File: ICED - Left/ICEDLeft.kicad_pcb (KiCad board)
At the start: 2 copper layers, 175.4 x 145 mm, 164 parts, among them P1 FLASH_HDR, P2 USBC, P3 CONN_17, P4 USB3_AFEMALE, Q1 TC1264, U1 MK20DX256VLH7, U2 IS31FL3731C, X1 CRYSTAL

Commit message: moved S23
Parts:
- moved D23 2.41 mm to (144.9, 94.6)
- moved D61 2.41 mm to (150.0, 97.7)
- moved S23 2.41 mm to (144.9, 97.7)
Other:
- outline, holes or cut-outs redrawn
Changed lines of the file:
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@@
   )
   (module prettylib:INSW_LEDS_REG (layer Front)
-    (at 149.987 100.086 270)
+    (at 149.9952 97.672 270)
     (attr smd)
     (fp_text reference D61 (at 0 -1.5 270) (layer B.SilkS)
@@
   )
   (module prettylib:SOT123-DIODE (layer Back)
-    (at 144.907 96.9745 90)
+    (at 144.9152 94.5605 90)
     (descr DIODE)
     (tags DIODE)
@@
   )
   (module prettylib:MXALPS (layer Front)
-    (at 144.907 100.086 90)
+    (at 144.9152 97.672 90)
     (descr MXALPS)
     (tags MXALPS)
@@
   (gr_line (start 170.053 170.815) (end 170.434 170.815) (angle 90) (layer Edge.Cuts) (width 0.127))
   (gr_line (start 193.04 122.301) (end 170.434 170.815) (angle 90) (layer Edge.Cuts) (width 0.127))
-  (gr_line (start 90.17 135.509) (end 94.361 135.509) (angle 90) (layer Edge.Cuts) (width 0.127))
-  (gr_line (start 170.053 170.815) (end 94.361 135.509) (angle 90) (layer Edge.Cuts) (width 0.127))
+  (gr_line (start 66.012873 135.509) (end 66.012873 164.658583) (angle 90) (layer Edge.Cuts) (width 0.127))
+  (gr_line (start 66.012873 164.658583) (end 94.361 170.815) (angle 90) (layer Edge.Cuts) (width 0.127))
   (gr_line (start 192.913 122.047) (end 154.813 104.267) (angle 90) (layer Edge.Cuts) (width 0.127))
-  (gr_line (start 90.17 135.509) (end 20.955 135.509) (angle 90) (layer Edge.Cuts) (width 0.127))
+  (gr_line (start 66.012873 135.509) (end 20.955 135.509) (angle 90) (layer Edge.Cuts) (width 0.127))
   (gr_line (start 64.897 27.559) (end 19.558 27.559) (angle 90) (layer Edge.Cuts) (width 0.127))
   (gr_line (start 64.897 32.639) (end 64.897 27.559) (angle 90) (layer Edge.Cuts) (width 0.127))

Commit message: moved LCD1
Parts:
- moved LCD1 135.8 mm to (157.6, 104.0), turned to 270 degrees
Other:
- outline, holes or cut-outs redrawn
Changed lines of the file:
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@@
   )
   (module prettylib:NHD-C12832A1Z (layer Front)
-    (at 38.497 38.615)
+    (at 157.58588 103.96079 270)
     (descr "NHD-C12832A1Z LCD")
     (tags "HDR SIL")
-    (fp_text reference LCD1 (at 23.098 -5.976) (layer F.SilkS)
+    (fp_text reference LCD1 (at 23.098 -5.976 90) (layer F.SilkS)
       (effects (font (size 1 1) (thickness 0.2)))
     )
-    (fp_text value NHD-C12832A1Z (at 0 2.1) (layer F.SilkS) hide
+    (fp_text value NHD-C12832A1Z (at 0 2.1 90) (layer F.SilkS) hide
       (effects (font (size 0.65 0.65) (thickness 0.0975)))
     )
@@
     (fp_line (start -20.7 -23.7) (end -20.7 0.6) (layer Dwgs.User) (width 0.3))
     (fp_line (start 20.7 0.6) (end 20.7 -23.7) (layer Dwgs.User) (width 0.3))
-    (pad 1 thru_hole rect (at -17.3 -1.95 90) (size 1.5 2.4) (drill oval 0.9 2) (layers *.Cu *.Mask F.SilkS)
+    (pad 1 thru_hole rect (at -17.3 -1.95 0) (size 1.5 2.4) (drill oval 0.9 2) (layers *.Cu *.Mask F.SilkS)
       (net 33 VDD))
-    (pad 2 thru_hole rect (at -14.3 -1.95 90) (size 1.5 2.4) (drill oval 0.9 2) (layers *.Cu *.Mask F.SilkS)
+    (pad 2 thru_hole rect (at -14.3 -1.95 0) (size 1.5 2.4) (drill oval 0.9 2) (layers *.Cu *.Mask F.SilkS)
       (net 89 "Net-(LCD1-Pad2)"))
-    (pad 3 thru_hole circle (at -12 0 90) (size 1.2 1.2) (drill 0.7) (layers *.Cu *.Mask F.SilkS)
+    (pad 3 thru_hole circle (at -12 0 0) (size 1.2 1.2) (drill 0.7) (layers *.Cu *.Mask F.SilkS)
       (net 48 "Net-(C17-Pad2)"))
-    (pad 4 thru_hole circle (at -10.5 0 90) (size 1.2 1.2) (drill 0.7) (layers *.Cu *.Mask F.SilkS)
+    (pad 4 thru_hole circle (at -10.5 0 0) (size 1.2 1.2) (drill 0.7) (layers *.Cu *.Mask F.SilkS)
       (net 47 "Net-(C16-Pad2)"))
-    (pad 5 thru_hole circle (at -9 0 90) (size 1.2 1.2) (drill 0.7) (layers *.Cu *.Mask F.SilkS)
+    (pad 5 thru_hole circle (at -9 0 0) (size 1.2 1.2) (drill 0.7) (layers *.Cu *.Mask F.SilkS)
       (net 46 "Net-(C15-Pad2)"))
-    (pad 6 thru_hole circle (at -7.5 0 90) (size 1.2 1.2) (drill 0.7) (layers *.Cu *.Mask F.SilkS)
+    (pad 6 thru_hole circle (at -7.5 0 0) (size 1.2 1.2) (drill 0.7) (layers *.Cu *.Mask F.SilkS)
       (net 45 "Net-(C14-Pad2)"))
-    (pad 7 thru_hole circle (at -6 0 90) (size 1.2 1.2) (drill 0.7) (layers *.Cu *.Mask F.SilkS)
+    (pad 7 thru_hole circle (at -6 0 0) (size 1.2 1.2) (drill 0.7) (layers *.Cu *.Mask F.SilkS)
       (net 44 "Net-(C13-Pad2)"))
-    (pad 8 thru_hole circle (at -4.5 0 90) (size 1.2 1.2) (drill 0.7) (layers *.Cu *.Mask F.SilkS)
+    (pad 8 thru_hole circle (at -4.5 0 0) (size 1.2 1.2) (drill 0.7) (layers *.Cu *.Mask F.SilkS)
       (net 43 "Net-(C12-Pad2)"))
-    (pad 9 thru_hole circle (at -3 0 90) (size 1.2 1.2) (drill 0.7) (layers *.Cu *.Mask F.SilkS)
+    (pad 9 thru_hole circle (at -3 0 0) (size 1.2 1.2) (drill 0.7) (layers *.Cu *.Mask F.SilkS)
       (net 42 "Net-(C12-Pad1)"))
-    (pad 10 thru_hole circle (at -1.5 0 90) (size 1.2 1.2) (drill 0.7) (layers *.Cu *.Mask F.SilkS)
+    (pad 10 thru_hole circle (at -1.5 0 0) (size 1.2 1.2) (drill 0.7) (layers *.Cu *.Mask F.SilkS)
       (net 41 "Net-(C11-Pad2)"))
-    (pad 11 thru_hole circle (at 0 0 90) (size 1.2 1.2) (drill 0.7) (layers *.Cu *.Mask F.SilkS)
+    (pad 11 thru_hole circle (at 0 0 0) (size 1.2 1.2) (drill 0.7) (layers *.Cu *.Mask F.SilkS)
       (net 40 "Net-(C11-Pad1)"))
-    (pad 12 thru_hole circle (at 1.5 0 90) (size 1.2 1.2) (drill 0.7) (layers *.Cu *.Mask F.SilkS)
+    (pad 12 thru_hole circle (at 1.5 0 0) (size 1.2 1.2) (drill 0.7) (layers *.Cu *.Mask F.SilkS)
       (net 39 "Net-(C10-Pad1)"))
-    (pad 13 thru_hole circle (at 3 0 90) (size 1.2 1.2) (drill 0.7) (layers *.Cu *.Mask F.SilkS)
+    (pad 13 thru_hole circle (at 3 0 0) (size 1.2 1.2) (drill 0.7) (layers *.Cu *.Mask F.SilkS)
       (net 34 VSS))
-    (pad 14 thru_hole circle (at 4.5 0 90) (size 1.2 1.2) (drill 0.7) (layers *.Cu *.Mask F.SilkS)
+    (pad 14 thru_hole circle (at 4.5 0 0) (size 1.2 1.2) (drill 0.7) (layers *.Cu *.Mask F.SilkS)
       (net 33 VDD))
-    (pad 15 thru_hole circle (at 6 0 90) (size 1.2 1.2) (drill 0.7) (layers *.Cu *.Mask F.SilkS)
+    (pad 15 thru_hole circle (at 6 0 0) (size 1.2 1.2) (drill 0.7) (layers *.Cu *.Mask F.SilkS)
       (net 16 /mcu/MOSI))
-    (pad 16 thru_hole circle (at 7.5 0 90) (size 1.2 1.2) (drill 0.7) (layers *.Cu *.Mask F.SilkS)
+    (pad 16 thru_hole circle (at 7.5 0 0) (size 1.2 1.2) (drill 0.7) (layers *.Cu *.Mask F.SilkS)
       (net 22 /mcu/SCLK))
-    (pad 17 thru_hole circle (at 9 0 90) (size 1.2 1.2) (drill 0.7) (layers *.Cu *.Mask F.SilkS)
+    (pad 17 thru_hole circle (at 9 0 0) (size 1.2 1.2) (drill 0.7) (layers *.Cu *.Mask F.SilkS)
       (net 11 /mcu/A0))
-    (pad 18 thru_hole circle (at 10.5 0 90) (size 1.2 1.2) (drill 0.7) (layers *.Cu *.Mask F.SilkS)
+    (pad 18 thru_hole circle (at 10.5 0 0) (size 1.2 1.2) (drill 0.7) (layers *.Cu *.Mask F.SilkS)
       (net 17 /mcu/RST))
-    (pad 19 thru_hole circle (at 12 0 90) (size 1.2 1.2) (drill 0.7) (layers *.Cu *.Mask F.SilkS)
+    (pad 19 thru_hole circle (at 12 0 0) (size 1.2 1.2) (drill 0.7) (layers *.Cu *.Mask F.SilkS)
       (net 25 /mcu/SS1))
-    (pad 20 thru_hole rect (at 14.3 -1.95 90) (size 1.5 2.4) (drill oval 0.9 2) (layers *.Cu *.Mask F.SilkS)
+    (pad 20 thru_hole rect (at 14.3 -1.95 0) (size 1.5 2.4) (drill oval 0.9 2) (layers *.Cu *.Mask F.SilkS)
       (net 90 "Net-(LCD1-Pad20)"))
-    (pad 21 thru_hole rect (at 17.3 -1.95 90) (size 1.5 2.4) (drill oval 0.9 2) (layers *.Cu *.Mask F.SilkS)
+    (pad 21 thru_hole rect (at 17.3 -1.95 0) (size 1.5 2.4) (drill oval 0.9 2) (layers *.Cu *.Mask F.SilkS)
       (net 91 "Net-(LCD1-Pad21)"))
-    (pad "" np_thru_hole circle (at 20.1 0 90) (size 0.85001 0.85001) (drill 0.85) (layers *.Cu *.Mask F.SilkS))
-    (pad "" np_thru_hole circle (at -20.1 0 90) (size 0.85001 0.85001) (drill 0.85) (layers *.Cu *.Mask F.SilkS))
+    (pad "" np_thru_hole circle (at 20.1 0 0) (size 0.85001 0.85001) (drill 0.85) (layers *.Cu *.Mask F.SilkS))
+    (pad "" np_thru_hole circle (at -20.1 0 0) (size 0.85001 0.85001) (drill 0.85) (layers *.Cu *.Mask F.SilkS))
     (model 3d/NHD-C12832A1Z.wrl
-      (at (xyz 0 -0.024 0.065))
+      (at (xyz 0 -0.024 270.065))
       (scale (xyz 0.393701 0.393701 0.393701))
-      (rotate (xyz 0 0 0))
+      (rotate (xyz 0 0 270))
     )
   )
@@
   (gr_line (start 17.653 29.464) (end 17.653 132.207) (angle 90) (layer Edge.Cuts) (width 0.127))
   (gr_line (start 193.04 122.301) (end 192.913 122.047) (angle 90) (layer Edge.Cuts) (width 0.127))
-  (gr_line (start 170.053 170.815) (end 170.434 170.815) (angle 90) (layer Edge.Cuts) (width 0.127))
-  (gr_line (start 193.04 122.301) (end 170.434 170.815) (angle 90) (layer Edge.Cuts) (width 0.127))
+  (gr_line (start 72.16929 170.815) (end 170.434 170.815) (angle 90) (layer Edge.Cuts) (width 0.127))
+  (gr_line (start 176.590417 164.658583) (end 170.434 170.815) (angle 90) (layer Edge.Cuts) (width 0.127))
   (gr_line (start 66.012873 135.509) (end 66.012873 164.658583) (angle 90) (layer Edge.Cuts) (width 0.127))
-  (gr_line (start 66.012873 164.658583) (end 94.361 170.815) (angle 90) (layer Edge.Cuts) (width 0.127))
+  (gr_line (start 66.012873 164.658583) (end 72.16929 170.815) (angle 90) (layer Edge.Cuts) (width 0.127))
   (gr_line (start 192.913 122.047) (end 154.813 104.267) (angle 90) (layer Edge.Cuts) (width 0.127))
   (gr_line (start 66.012873 135.509) (end 20.955 135.509) (angle 90) (layer Edge.Cuts) (width 0.127))

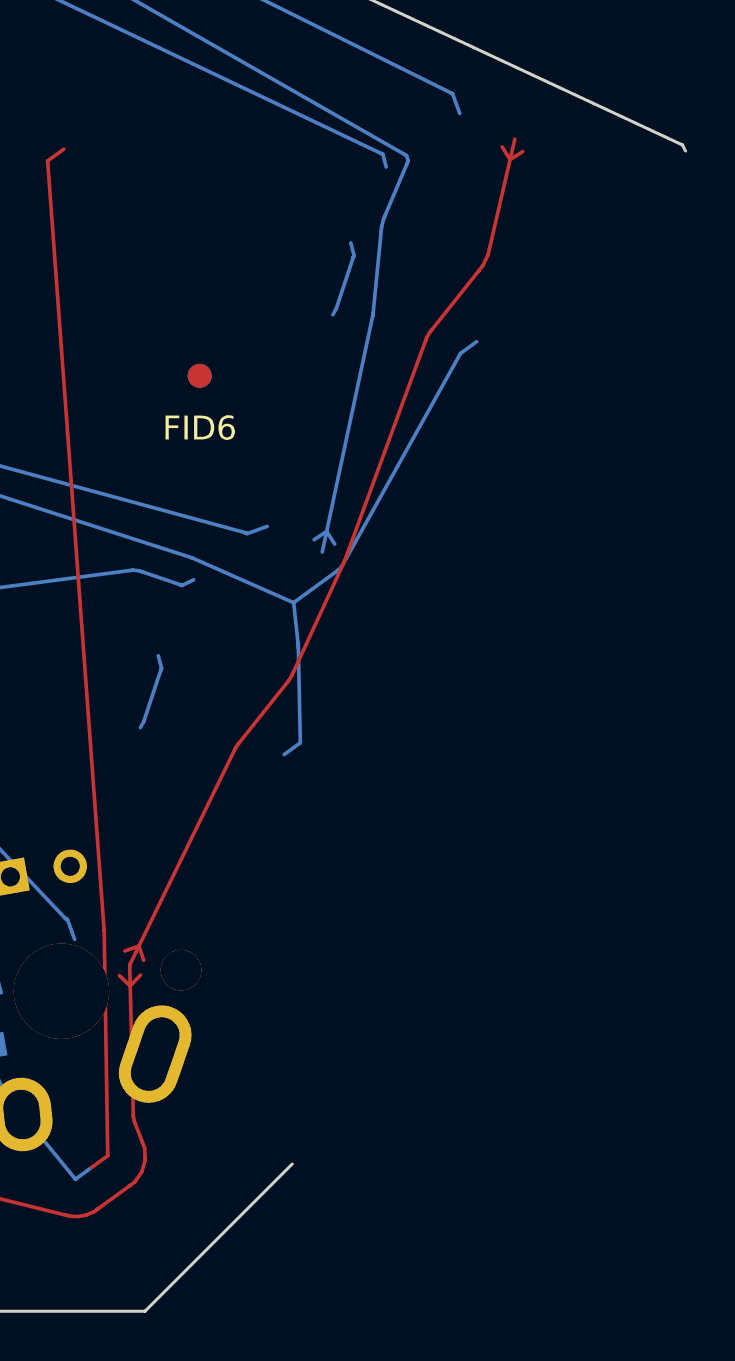
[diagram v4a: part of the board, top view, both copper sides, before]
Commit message: moved a few edge cuts
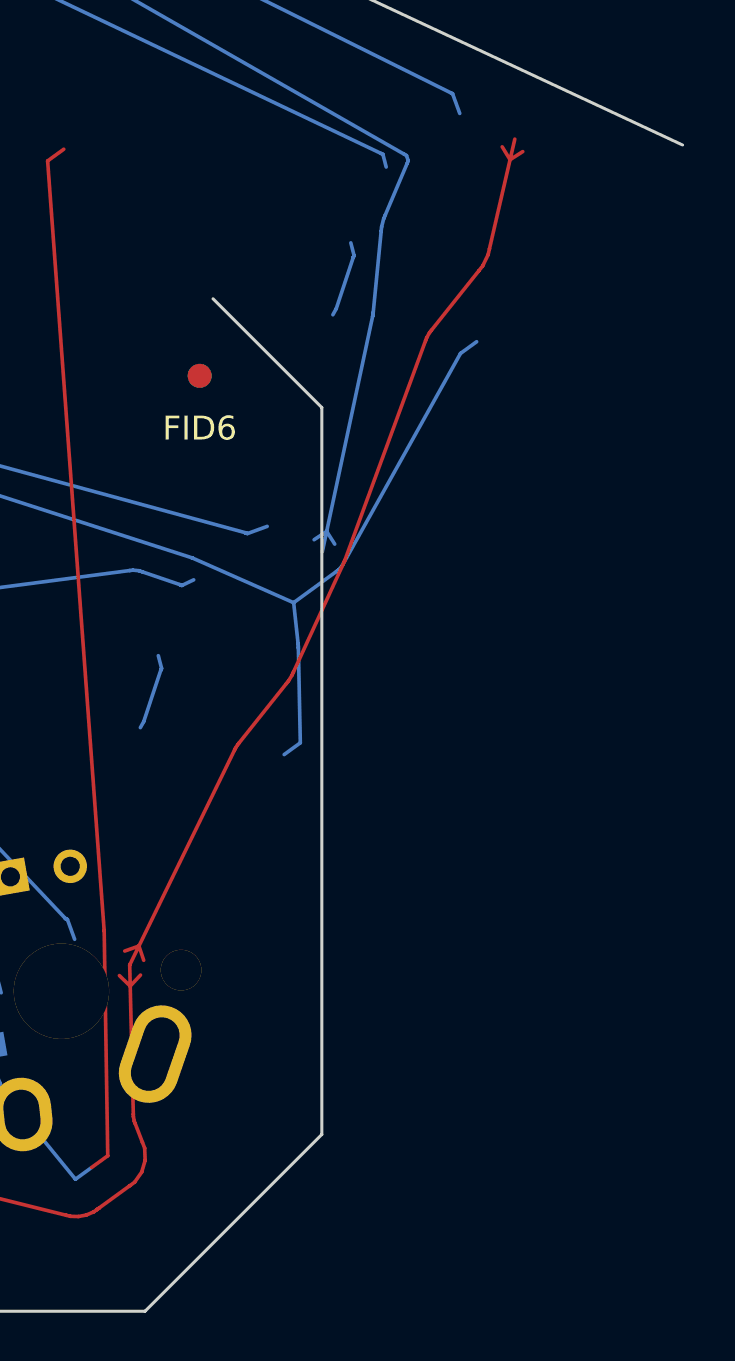
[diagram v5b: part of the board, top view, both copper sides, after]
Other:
- board size 175.4 x 145 mm -> 175.3 x 145 mm
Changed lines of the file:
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@@
   (gr_line (start 17.653 132.207) (end 20.955 135.509) (angle 90) (layer Edge.Cuts) (width 0.127))
   (gr_line (start 17.653 29.464) (end 17.653 132.207) (angle 90) (layer Edge.Cuts) (width 0.127))
-  (gr_line (start 193.04 122.301) (end 192.913 122.047) (angle 90) (layer Edge.Cuts) (width 0.127))
+  (gr_line (start 177.828 133.026) (end 173.279 128.477) (angle 90) (layer Edge.Cuts) (width 0.127))
+  (gr_line (start 177.828 163.422) (end 177.828 133.026) (angle 90) (layer Edge.Cuts) (width 0.127))
   (gr_line (start 72.16929 170.815) (end 170.434 170.815) (angle 90) (layer Edge.Cuts) (width 0.127))
-  (gr_line (start 176.590417 164.658583) (end 170.434 170.815) (angle 90) (layer Edge.Cuts) (width 0.127))
+  (gr_line (start 177.828 163.422) (end 170.434 170.815) (angle 90) (layer Edge.Cuts) (width 0.127))
   (gr_line (start 66.012873 135.509) (end 66.012873 164.658583) (angle 90) (layer Edge.Cuts) (width 0.127))
   (gr_line (start 66.012873 164.658583) (end 72.16929 170.815) (angle 90) (layer Edge.Cuts) (width 0.127))
